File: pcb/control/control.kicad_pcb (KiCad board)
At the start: 2 copper layers, 68 x 76 mm, 64 parts, among them J1 Conn_01x06, J2 Conn_01x05, J3 Conn_01x01, J4 USB_B_Micro, J5 Conn_01x04, J7 Conn_01x02, J8 Conn_01x02, SW1 PEC12R-4217F-S0024, U1 E73-2G4M08S1C-52840, U10 DCX114YU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

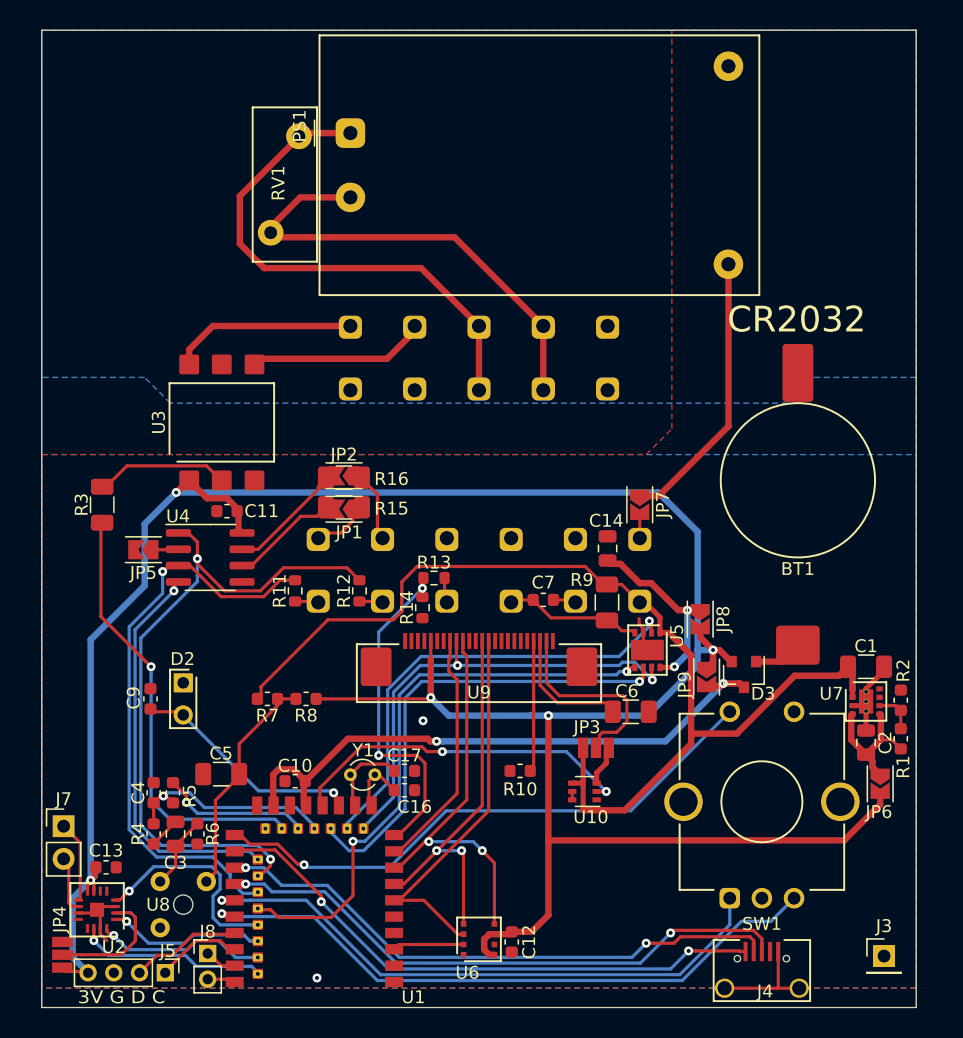
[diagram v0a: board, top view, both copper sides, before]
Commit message: Add FeRam and extension header to pcb
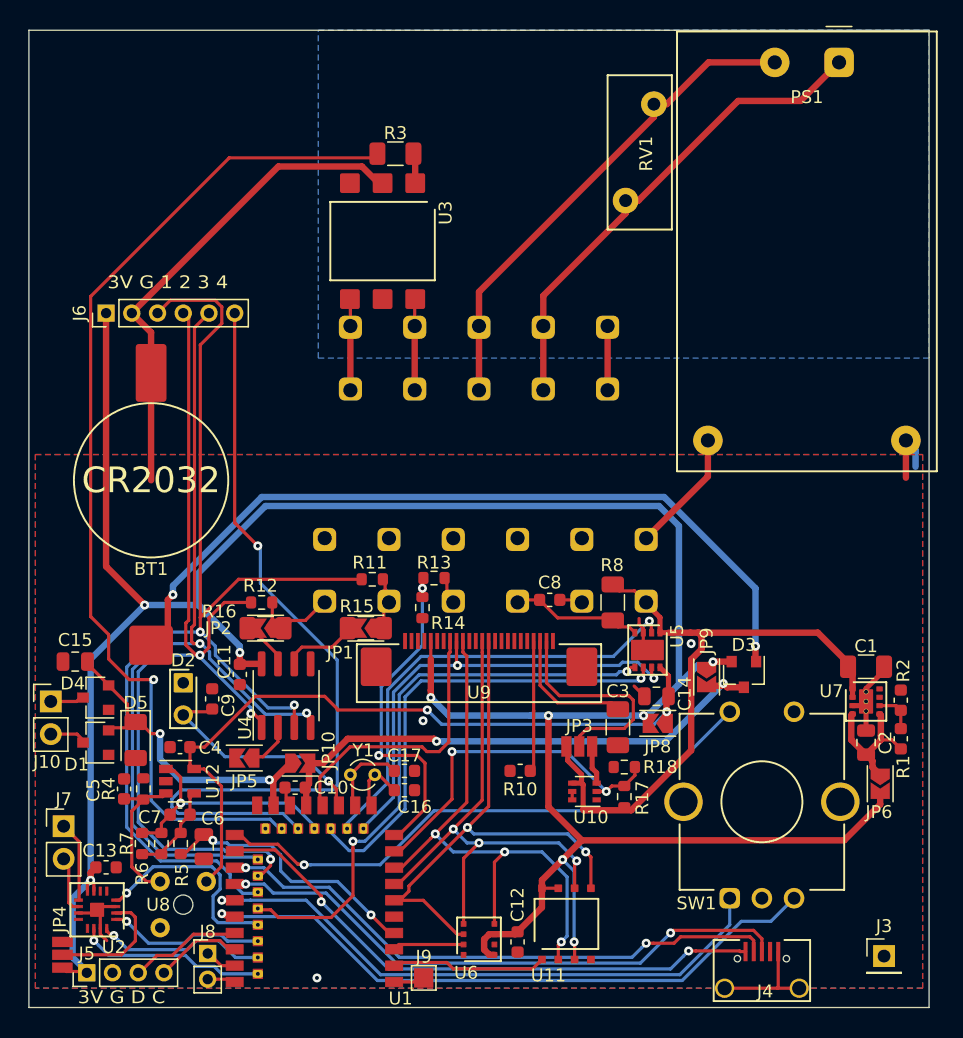
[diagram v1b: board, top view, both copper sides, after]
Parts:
- removed JP7: SolderJumper_2_Open, RoomControl:Jumper2
- removed the R8 at (86.5, 114.0)
- added C15: 22u/6V3, Capacitor_SMD:C_0805_2012Metric, F.Cu at (68.6, 111.1)
- added C7: 10n, Capacitor_SMD:C_0603_1608Metric, F.Cu at (76.8, 123.0)
- added D1: BAS40-04, Package_TO_SOT_SMD:SOT-23, F.Cu at (70.2, 117.4)
- added D4: BAS40-04, Package_TO_SOT_SMD:SOT-23, F.Cu at (70.2, 113.9)
- added D5: D_Zener_Small, Diode_SMD:D_1206_3216Metric, F.Cu at (73.3, 117.2)
- added J10: Conn_01x02, Connector_PinHeader_2.54mm:PinHeader_1x02_P2.54mm_Vertical, F.Cu at (66.7, 114.2)
- added J6: Conn_01x06, Connector_PinHeader_2.00mm:PinHeader_1x06_P2.00mm_Vertical, F.Cu at (71.0, 84.0)
- added J9: Conn_01x01, TestPoint:TestPoint_Pad_1.5x1.5mm, F.Cu at (95.7, 135.7)
- added JP10: SolderJumper_2_Open, RoomControl:Jumper2, F.Cu at (86.1, 119.0)
- added R17: 47k, Resistor_SMD:R_0603_1608Metric, F.Cu at (111.3, 121.6)
- added R18: 10k, Resistor_SMD:R_0603_1608Metric, F.Cu at (111.3, 119.3)
- added U11: MR45V064B, RoomControl:MR45V064B, F.Cu at (106.8, 131.5)
- added U12: MCP6001-OT, Package_TO_SOT_SMD:SOT-23-5, F.Cu at (76.8, 120.4)
- C1: value 10u/25V/X7R -> 10u/16V
- C14, C2: value 22u/16V -> 22u/6V3
- C3: value 22u/16V -> 10u/16V; footprint Capacitor_SMD:C_0805_2012Metric -> Capacitor_SMD:C_1206_3216Metric
- C5: value 10u/25V/X7R -> 10n; footprint Capacitor_SMD:C_1206_3216Metric -> Capacitor_SMD:C_0603_1608Metric
- C6: value 10u/25V/X7R -> 22u/6V3; footprint Capacitor_SMD:C_1206_3216Metric -> Capacitor_SMD:C_0805_2012Metric
- R4: value 10k -> 33k
- R5: value 10M -> 33k
- R6, R7: value 33k -> 10M
- moved BT1 50.3 mm to (74.5, 97.0)
- moved PS1 38.4 mm to (128.0, 64.5), turned to 270 degrees
- moved R3 35.6 mm to (93.5, 71.6), turned to 0 degrees
- moved C3 35.4 mm to (110.8, 116.2)
- moved C6 34.8 mm to (78.6, 125.5), turned to 90 degrees
- moved RV1 27.7 mm to (112.5, 71.5), turned to 90 degrees
- moved U3 18.8 mm to (92.5, 78.4), turned to 270 degrees
- moved JP5 18.0 mm to (81.8, 118.6)
- moved R7 14.9 mm to (73.8, 125.2), turned to 90 degrees
- moved JP2 13.3 mm to (83.4, 108.5)
- moved R16 13.2 mm to (83.4, 108.5)
- moved C11 12.7 mm to (81.4, 112.1), turned to 90 degrees
- moved U4 12.3 mm to (85.0, 113.8), turned to 90 degrees
- moved C14 12.1 mm to (113.8, 113.8), turned to 0 degrees
- moved R15 9.55 mm to (91.2, 108.5)
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- renumbered C7 to C8, R9 to R8
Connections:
- C14 pad 2: Net-(C14-Pad2) -> +3.3VA
- C3 pad 2: Net-(C3-Pad2) -> GND
- C4 pad 2: MD_COMP -> +3.3VA
- C5 pad 1: Net-(C5-Pad1) -> GND
- C5 pad 2: GND -> Net-(C5-Pad2)
- C6 pad 1: Net-(C6-Pad1) -> GND
- C6 pad 2: GND -> MD_N
- J1 pad 1: EXT1 -> EXT2
- J1 pad 2: EXT2 -> EXT1
- J5 pad 1: SWDCLK -> +3V3
- J5 pad 2: SWDIO -> GND
- J5 pad 3: GND -> SWDIO
- J5 pad 4: +3V3 -> SWDCLK
- JP8 pad 1: Net-(C14-Pad2) -> +3.3VA
- PS1 pad 1: L -> N
- PS1 pad 2: N -> L
- PS1 pad 4: Net-(JP7-Pad1) -> +12V
- R4 pad 1: Net-(C3-Pad1) -> GND
- R4 pad 2: MD_COMP -> Net-(C5-Pad2)
- R5 pad 1: MD_COMP -> MD_N
- R5 pad 2: MD_DS -> Net-(C7-Pad1)
- R6 pad 1: GND -> Net-(C7-Pad1)
- R6 pad 2: Net-(C3-Pad2) -> MD_P
- R7 pad 1: Net-(C5-Pad1) -> Net-(C7-Pad1)
- R7 pad 2: +12V -> MD_P
- RV1 pad 1: L -> N
- RV1 pad 2: N -> L
- U1 pad 17: EN_12V -> DISP_CS
- U1 pad 18: MD_COMP -> MD_P
- U1 pad 2: Net-(U1-Pad2) -> FERAM_CS
- U1 pad 20: MD_DS -> PIN4
- U1 pad 23: Net-(C10-Pad1) -> Net-(C15-Pad2)
- U1 pad 4: Net-(U1-Pad4) -> MD_N
- U1 pad 9: DISP_CS -> EN_12V
- U3 pad 1: +3V3 -> Net-(R3-Pad2)
- U3 pad 2: Net-(R3-Pad2) -> GND
- U3 pad 4: H2 -> H1
- U3 pad 6: H1 -> H2
- U5 pad 8: Net-(C14-Pad2) -> +3.3VA
- U8 pad 1: Net-(C5-Pad1) -> +3.3VA
- U8 pad 2: Net-(C3-Pad2) -> Net-(C5-Pad2)
- U9 pad 22: Net-(C6-Pad1) -> Net-(C3-Pad1)
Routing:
- net PIN4: track 0.00 -> 64.5 mm, vias 0 -> 1
- net Net-(BT1-Pad1): track 3.78 -> 62.1 mm, vias 0 -> 2
- net +3.3VA: track 0.00 -> 57.2 mm, vias 0 -> 2
- net GND: track 25.5 -> 72.0 mm, vias 2 -> 3
- net H: track 34.7 -> 80.1 mm
- net PIN1: track 45.5 -> 89.2 mm, vias 1 -> 2
- net PIN3: track 31.1 -> 68.0 mm, vias 1 -> 2
- net Net-(C15-Pad2): track 0.00 -> 26.5 mm, vias 0 -> 2
- net +12V: track 85.2 -> 59.9 mm
- net Net-(JP7-Pad1): track 21.7 -> 0.00 mm
- net MD_N: track 0.00 -> 21.6 mm, vias 0 -> 2
- net MD_P: track 0.00 -> 19.1 mm, vias 0 -> 1
- net PIN2: track 53.9 -> 73.0 mm, vias 2 -> 3
- net Net-(C5-Pad1): track 17.9 -> 0.00 mm
- net +3V3: track 200.7 -> 218.5 mm, vias 5 -> 9
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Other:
- board size 68 x 76 mm -> 70 x 76 mm
- board text added: "3V G 1 2 3 4"

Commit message: Test circuit for generator, switch: LEDs at center
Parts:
- added D6: D_Small, Diode_SMD:D_1206_3216Metric_Castellated, B.Cu at (77.8, 102.2)
- added D7: D_Small, Diode_SMD:D_1206_3216Metric_Castellated, B.Cu at (75.6, 102.2)
- added D8: D_Small, Diode_SMD:D_1206_3216Metric_Castellated, B.Cu at (77.8, 97.2)
- added D9: D_Small, Diode_SMD:D_1206_3216Metric_Castellated, B.Cu at (75.6, 97.2)
- J6: footprint Connector_PinHeader_2.00mm:PinHeader_1x06_P2.00mm_Vertical -> Connector_PinHeader_2.54mm:PinHeader_1x06_P2.54mm_Vertical
- R11, R12, R13: footprint Resistor_SMD:R_0603_1608Metric -> Resistor_SMD:R_1206_3216Metric
- moved R12 1.53 mm to (84.6, 106.2)
- moved J6 1.00 mm to (70.0, 84.0)
- moved J10 0.60 mm to (67.3, 114.2)
- moved R11 0.45 mm to (91.5, 104.3)
- moved R13 0.36 mm to (96.7, 104.3)
- moved D1 0.25 mm to (70.5, 117.4)
- moved D4 0.25 mm to (70.5, 113.9)
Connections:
- net Net-(C15-Pad2) renamed GENERATOR
- net Net-(D1-Pad3) renamed G1
- net Net-(D4-Pad3) renamed G2
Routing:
- net G1: track 2.69 -> 25.9 mm
- net G2: track 2.71 -> 21.7 mm
- net GENERATOR: track 26.5 -> 39.0 mm, vias 2 -> 3
- net PIN1: track 89.2 -> 90.6 mm
- net H: track 80.1 -> 81.2 mm
- net EXT2: track 7.58 -> 6.59 mm
- net PIN2: track 73.0 -> 73.9 mm
- net Net-(BT1-Pad1): track 62.1 -> 63.1 mm
- net AD: track 26.8 -> 27.7 mm
- net PIN4: track 64.5 -> 63.7 mm
- net GND: track 72.0 -> 72.7 mm

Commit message: 1st prototype of pcb
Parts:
- D5: footprint Diode_SMD:D_1206_3216Metric -> Diode_SMD:D_SOD-323F
- U11: value MR45V064B -> FM25CL64B
